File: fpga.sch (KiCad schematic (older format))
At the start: 25 parts, among them IC1 EP4CE10F17, J1 Pinheader_2x5_TH_WALL, U21 EPCS4

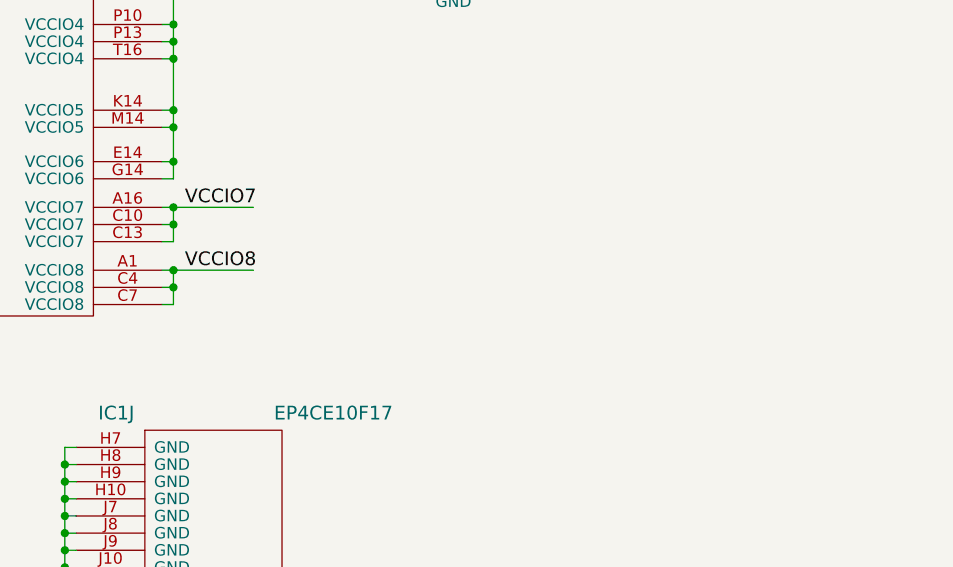
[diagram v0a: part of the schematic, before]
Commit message: Start fitting DDR2
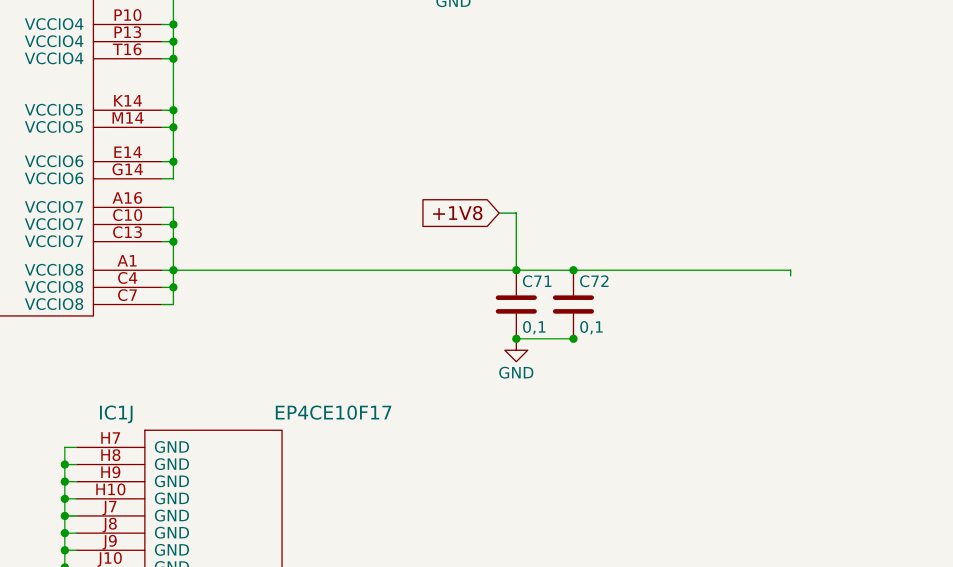
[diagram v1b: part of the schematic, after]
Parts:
- added C71, C72: 0,1, Capacitors_SMD:C_0603, symbol C
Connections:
- net labels added: +1V8
- net labels removed: VCCIO7, VCCIO8
- wire segments 160 -> 163
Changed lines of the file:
@@
 LIBS:Stream
 LIBS:ep4ce10f17
+LIBS:Winbond
 LIBS:Sputnik-cache
 EELAYER 25 0
@@
 $EndComp
 $Comp
-L GND #PWR01
+L GND #PWR6
 U 1 1 5807C448
 P 12075 6725
-F 0 "#PWR01" H 12075 6475 50  0001 C CNN
+F 0 "#PWR6" H 12075 6475 50  0001 C CNN
 F 1 "GND" H 12075 6575 50  0000 C CNN
 F 2 "" H 12075 6725 50  0000 C CNN
@@
 Text GLabel 10525 1600 1    60   Input ~ 0
 VCCINT
-Text Label 12600 3375 0    60   ~ 0
-VCCIO7
-Text Label 12600 3650 0    60   ~ 0
-VCCIO8
 Text Label 10325 3025 0    60   ~ 0
 VCCA1
@@
 $EndComp
 $Comp
-L GND #PWR02
+L GND #PWR5
 U 1 1 57F7A288
 P 2675 3000
-F 0 "#PWR02" H 2675 2750 50  0001 C CNN
+F 0 "#PWR5" H 2675 2750 50  0001 C CNN
 F 1 "GND" H 2675 2850 50  0000 C CNN
 F 2 "" H 2675 3000 50  0000 C CNN
@@
 NoConn ~ 2600 2775
 $Comp
-L +3V3 #PWR03
+L +3V3 #PWR8
 U 1 1 57F8D5C6
 P 13775 2025
-F 0 "#PWR03" H 13875 2075 20  0001 C CNN
+F 0 "#PWR8" H 13875 2075 20  0001 C CNN
 F 1 "+3V3" H 13775 2115 30  0000 C CNN
 F 2 "" H 13775 2025 60  0000 C CNN
@@
 $EndComp
 $Comp
-L GND #PWR04
+L GND #PWR9
 U 1 1 57F8FD8F
 P 13775 2325
-F 0 "#PWR04" H 13775 2075 50  0001 C CNN
+F 0 "#PWR9" H 13775 2075 50  0001 C CNN
 F 1 "GND" H 13775 2175 50  0000 C CNN
 F 2 "" H 13775 2325 50  0000 C CNN
@@
 $EndComp
 $Comp
-L GND #PWR05
+L GND #PWR7
 U 1 1 57F90743
 P 13275 1400
-F 0 "#PWR05" H 13275 1150 50  0001 C CNN
+F 0 "#PWR7" H 13275 1150 50  0001 C CNN
 F 1 "GND" H 13275 1250 50  0000 C CNN
 F 2 "" H 13275 1400 50  0000 C CNN
@@
 Connection ~ 12550 3175
 Wire Wire Line
-	12500 3375 12900 3375
-Wire Wire Line
-	12500 3650 12900 3650
+	12500 3650 15250 3650
 Wire Wire Line
 	12550 3525 12500 3525
 Wire Wire Line
-	12550 3375 12550 3525
-Connection ~ 12550 3375
+	12550 3375 12550 3800
 Wire Wire Line
 	12500 3450 12550 3450
@@
 Wire Wire Line
 	12550 3800 12500 3800
-Wire Wire Line
-	12550 3650 12550 3800
 Connection ~ 12550 3650
 Wire Wire Line
@@
 $EndComp
 $Comp
-L GND #PWR06
+L GND #PWR2
 U 1 1 58612A86
 P 1700 4125
-F 0 "#PWR06" H 1700 3875 50  0001 C CNN
+F 0 "#PWR2" H 1700 3875 50  0001 C CNN
 F 1 "GND" H 1700 3975 50  0000 C CNN
 F 2 "" H 1700 4125 50  0000 C CNN
@@
 $EndComp
 $Comp
-L +3V3 #PWR07
+L +3V3 #PWR3
 U 1 1 586140D5
 P 2650 3775
-F 0 "#PWR07" H 2750 3825 20  0001 C CNN
+F 0 "#PWR3" H 2750 3825 20  0001 C CNN
 F 1 "+3V3" H 2650 3865 30  0000 C CNN
 F 2 "" H 2650 3775 60  0000 C CNN
@@
 Connection ~ 2650 3825
 $Comp
-L +3V3 #PWR08
+L +3V3 #PWR1
 U 1 1 58614C3F
 P 1575 4025
-F 0 "#PWR08" H 1675 4075 20  0001 C CNN
+F 0 "#PWR1" H 1675 4075 20  0001 C CNN
 F 1 "+3V3" H 1575 4115 30  0000 C CNN
 F 2 "" H 1575 4025 60  0000 C CNN
@@
 $EndComp
 $Comp
-L GND #PWR09
+L GND #PWR4
 U 1 1 586161B6
 P 2650 4500
-F 0 "#PWR09" H 2650 4250 50  0001 C CNN
+F 0 "#PWR4" H 2650 4250 50  0001 C CNN
 F 1 "GND" H 2650 4350 50  0000 C CNN
 F 2 "" H 2650 4500 50  0000 C CNN
@@
 Text Label 7050 6050 2    50   ~ 0
 ETHSD14
+$Comp
+L C C71
+U 1 1 5883464A
+P 14050 3800
+F 0 "C71" H 14075 3900 50  0000 L CNN
+F 1 "0,1" H 14075 3700 50  0000 L CNN
+F 2 "Capacitors_SMD:C_0603" H 14088 3650 50  0001 C CNN
+F 3 "" H 14050 3800 50  0000 C CNN
+	1    14050 3800
+	1    0    0    -1
+$EndComp
+$Comp
+L GND #PWR10
+U 1 1 5883481A
+P 14050 3950
+F 0 "#PWR10" H 14050 3700 50  0001 C CNN
+F 1 "GND" H 14050 3800 50  0000 C CNN
+F 2 "" H 14050 3950 50  0000 C CNN
+F 3 "" H 14050 3950 50  0000 C CNN
+	1    14050 3950
+	1    0    0    -1
+$EndComp
+Wire Wire Line
+	15250 3650 15250 3675
+Connection ~ 14050 3650
+Text GLabel 13975 3400 0    60   Input ~ 0
++1V8
+Wire Wire Line
+	13975 3400 14050 3400
+Wire Wire Line
+	14050 3400 14050 3650
+Wire Wire Line
+	12500 3375 12550 3375
+Connection ~ 12550 3525
+$Comp
+L C C72
+U 1 1 588362E2
+P 14300 3800
+F 0 "C72" H 14325 3900 50  0000 L CNN
+F 1 "0,1" H 14325 3700 50  0000 L CNN
+F 2 "Capacitors_SMD:C_0603" H 14338 3650 50  0001 C CNN
+F 3 "" H 14300 3800 50  0000 C CNN
+	1    14300 3800
+	1    0    0    -1
+$EndComp
+Wire Wire Line
+	14300 3950 14050 3950
+Connection ~ 14050 3950
+Connection ~ 14300 3950
+Connection ~ 14300 3650
 $EndSCHEMATC

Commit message: A bit of routing
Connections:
- net labels added: USBAD[0:15]
- net labels removed: VREFB3N0, VREFB4N0, VREFB5N0
- wire segments 163 -> 155
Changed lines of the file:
@@
 $EndComp
 $Comp
-L GND #PWR10
+L GND #PWR01
 U 1 1 5807C448
 P 12075 6725
-F 0 "#PWR10" H 12075 6475 50  0001 C CNN
+F 0 "#PWR01" H 12075 6475 50  0001 C CNN
 F 1 "GND" H 12075 6575 50  0000 C CNN
 F 2 "" H 12075 6725 50  0000 C CNN
@@
 $EndComp
 $Comp
-L GND #PWR4
+L GND #PWR02
 U 1 1 57F7A288
 P 2675 3000
-F 0 "#PWR4" H 2675 2750 50  0001 C CNN
+F 0 "#PWR02" H 2675 2750 50  0001 C CNN
 F 1 "GND" H 2675 2850 50  0000 C CNN
 F 2 "" H 2675 3000 50  0000 C CNN
@@
 NoConn ~ 2600 2775
 $Comp
-L +3V3 #PWR2
+L +3V3 #PWR03
 U 1 1 57F8D5C6
 P 13775 2025
-F 0 "#PWR2" H 13875 2075 20  0001 C CNN
+F 0 "#PWR03" H 13875 2075 20  0001 C CNN
 F 1 "+3V3" H 13775 2115 30  0000 C CNN
 F 2 "" H 13775 2025 60  0000 C CNN
@@
 	1    0    0    -1
 $EndComp
-Text Label 10050 6775 0    60   ~ 0
-VREFB4N0
-Text Label 9525 4625 0    60   ~ 0
-VREFB3N0
 Text Label 9150 2675 0    60   ~ 0
 VREFB2N0
@@
 $EndComp
 $Comp
-L GND #PWR3
+L GND #PWR04
 U 1 1 57F8FD8F
 P 13775 2325
-F 0 "#PWR3" H 13775 2075 50  0001 C CNN
+F 0 "#PWR04" H 13775 2075 50  0001 C CNN
 F 1 "GND" H 13775 2175 50  0000 C CNN
 F 2 "" H 13775 2325 50  0000 C CNN
@@
 $EndComp
 $Comp
-L GND #PWR1
+L GND #PWR05
 U 1 1 57F90743
 P 13275 1400
-F 0 "#PWR1" H 13275 1150 50  0001 C CNN
+F 0 "#PWR05" H 13275 1150 50  0001 C CNN
 F 1 "GND" H 13275 1250 50  0000 C CNN
 F 2 "" H 13275 1400 50  0000 C CNN
@@
 	1    0    0    -1
 $EndComp
-Text Label 9800 8675 0    60   ~ 0
-VREFB5N0
 $Comp
 L C C38
@@
 $EndComp
 $Comp
-L GND #PWR8
+L GND #PWR06
 U 1 1 58612A86
 P 1700 4125
-F 0 "#PWR8" H 1700 3875 50  0001 C CNN
+F 0 "#PWR06" H 1700 3875 50  0001 C CNN
 F 1 "GND" H 1700 3975 50  0000 C CNN
 F 2 "" H 1700 4125 50  0000 C CNN
@@
 $EndComp
 $Comp
-L +3V3 #PWR5
+L +3V3 #PWR07
 U 1 1 586140D5
 P 2650 3775
-F 0 "#PWR5" H 2750 3825 20  0001 C CNN
+F 0 "#PWR07" H 2750 3825 20  0001 C CNN
 F 1 "+3V3" H 2650 3865 30  0000 C CNN
 F 2 "" H 2650 3775 60  0000 C CNN
@@
 Connection ~ 2650 3825
 $Comp
-L +3V3 #PWR7
+L +3V3 #PWR08
 U 1 1 58614C3F
 P 1575 4025
-F 0 "#PWR7" H 1675 4075 20  0001 C CNN
+F 0 "#PWR08" H 1675 4075 20  0001 C CNN
 F 1 "+3V3" H 1575 4115 30  0000 C CNN
 F 2 "" H 1575 4025 60  0000 C CNN
@@
 $EndComp
 $Comp
-L GND #PWR9
+L GND #PWR09
 U 1 1 586161B6
 P 2650 4500
-F 0 "#PWR9" H 2650 4250 50  0001 C CNN
+F 0 "#PWR09" H 2650 4250 50  0001 C CNN
 F 1 "GND" H 2650 4350 50  0000 C CNN
 F 2 "" H 2650 4500 50  0000 C CNN
@@
 Text Label 7050 8550 2    50   ~ 0
 CMD
-Text Label 7050 7425 2    50   ~ 0
-ETHSD8
-Text Label 7050 8100 2    50   ~ 0
-ETHSD9
-Text Label 7050 7500 2    50   ~ 0
-ETHSD10
-Text Label 7050 8775 2    50   ~ 0
-ETHSD11
-Text Label 7050 8850 2    50   ~ 0
-ETHSD12
-Text Label 7050 8700 2    50   ~ 0
-ETHSD13
 Wire Bus Line
 	15100 6725 15100 7925
-Entry Wire Line
-	15100 6925 15200 7025
-Wire Wire Line
-	15200 7025 15600 7025
-Entry Wire Line
-	15100 7025 15200 7125
-Entry Wire Line
-	15100 7125 15200 7225
-Entry Wire Line
-	15100 7225 15200 7325
-Entry Wire Line
-	15100 7325 15200 7425
-Entry Wire Line
-	15100 7425 15200 7525
-Entry Wire Line
-	15100 7525 15200 7625
-Entry Wire Line
-	15100 7625 15200 7725
-Wire Wire Line
-	15200 7125 15600 7125
-Wire Wire Line
-	15200 7225 15600 7225
-Wire Wire Line
-	15200 7325 15600 7325
-Wire Wire Line
-	15200 7425 15600 7425
-Wire Wire Line
-	15200 7525 15600 7525
-Wire Wire Line
-	15200 7625 15600 7625
-Wire Wire Line
-	15200 7725 15600 7725
-Text Label 15600 7225 2    50   ~ 0
-ETHSD13
-Text Label 15600 7325 2    50   ~ 0
-ETHSD12
-Text Label 15600 7425 2    50   ~ 0
-ETHSD11
-Text Label 15600 7525 2    50   ~ 0
-ETHSD10
-Text Label 7050 6425 2    50   ~ 0
-ETHSD7
-Text Label 7050 5450 2    50   ~ 0
-ETHSD6
-Text Label 7050 5375 2    50   ~ 0
-ETHSD5
-Text Label 7050 5300 2    50   ~ 0
-ETHSD4
-Text Label 7050 6950 2    50   ~ 0
-ETHSD3
-Text Label 7050 6875 2    50   ~ 0
-ETHSD2
-Text Label 7050 7875 2    50   ~ 0
-ETHSD1
-Text Label 7050 6125 2    50   ~ 0
-ETHSD0
-Text Label 7050 8325 2    50   ~ 0
-ETHSD15
-Text Label 7050 6050 2    50   ~ 0
-ETHSD14
 $Comp
 L C C71
@@
 $EndComp
 $Comp
-L GND #PWR6
+L GND #PWR010
 U 1 1 5883481A
 P 14050 3950
-F 0 "#PWR6" H 14050 3700 50  0001 C CNN
+F 0 "#PWR010" H 14050 3700 50  0001 C CNN
 F 1 "GND" H 14050 3800 50  0000 C CNN
 F 2 "" H 14050 3950 50  0000 C CNN
@@
 Connection ~ 14300 3950
 Connection ~ 14300 3650
+Text HLabel 15100 8275 2    60   BiDi ~ 0
+USBAD[0:15]
+Text GLabel 7050 8850 0    39   Input ~ 0
+ETHSD12
+Text GLabel 7050 8775 0    39   Input ~ 0
+ETHSD11
+Text GLabel 7050 8700 0    39   Input ~ 0
+ETHSD13
+Text GLabel 7050 8325 0    39   Input ~ 0
+ETHSD15
+Text GLabel 7050 7500 0    39   Input ~ 0
+ETHSD10
+Text GLabel 7050 7875 0    39   Input ~ 0
+ETHSD1
+Text GLabel 7050 8100 0    39   Input ~ 0
+ETHSD9
+Text GLabel 7050 7425 0    39   Input ~ 0
+ETHSD8
+Text GLabel 7050 6950 0    39   Input ~ 0
+ETHSD3
+Text GLabel 7050 6875 0    39   Input ~ 0
+ETHSD2
+Text GLabel 7050 6425 0    39   Input ~ 0
+ETHSD7
+Text GLabel 7050 6125 0    39   Input ~ 0
+ETHSD0
+Text GLabel 7050 6050 0    39   Input ~ 0
+ETHSD14
+Text GLabel 7050 5450 0    39   Input ~ 0
+ETHSD6
+Text GLabel 7050 5375 0    39   Input ~ 0
+ETHSD5
+Text GLabel 7050 5300 0    39   Input ~ 0
+ETHSD4
 $EndSCHEMATC

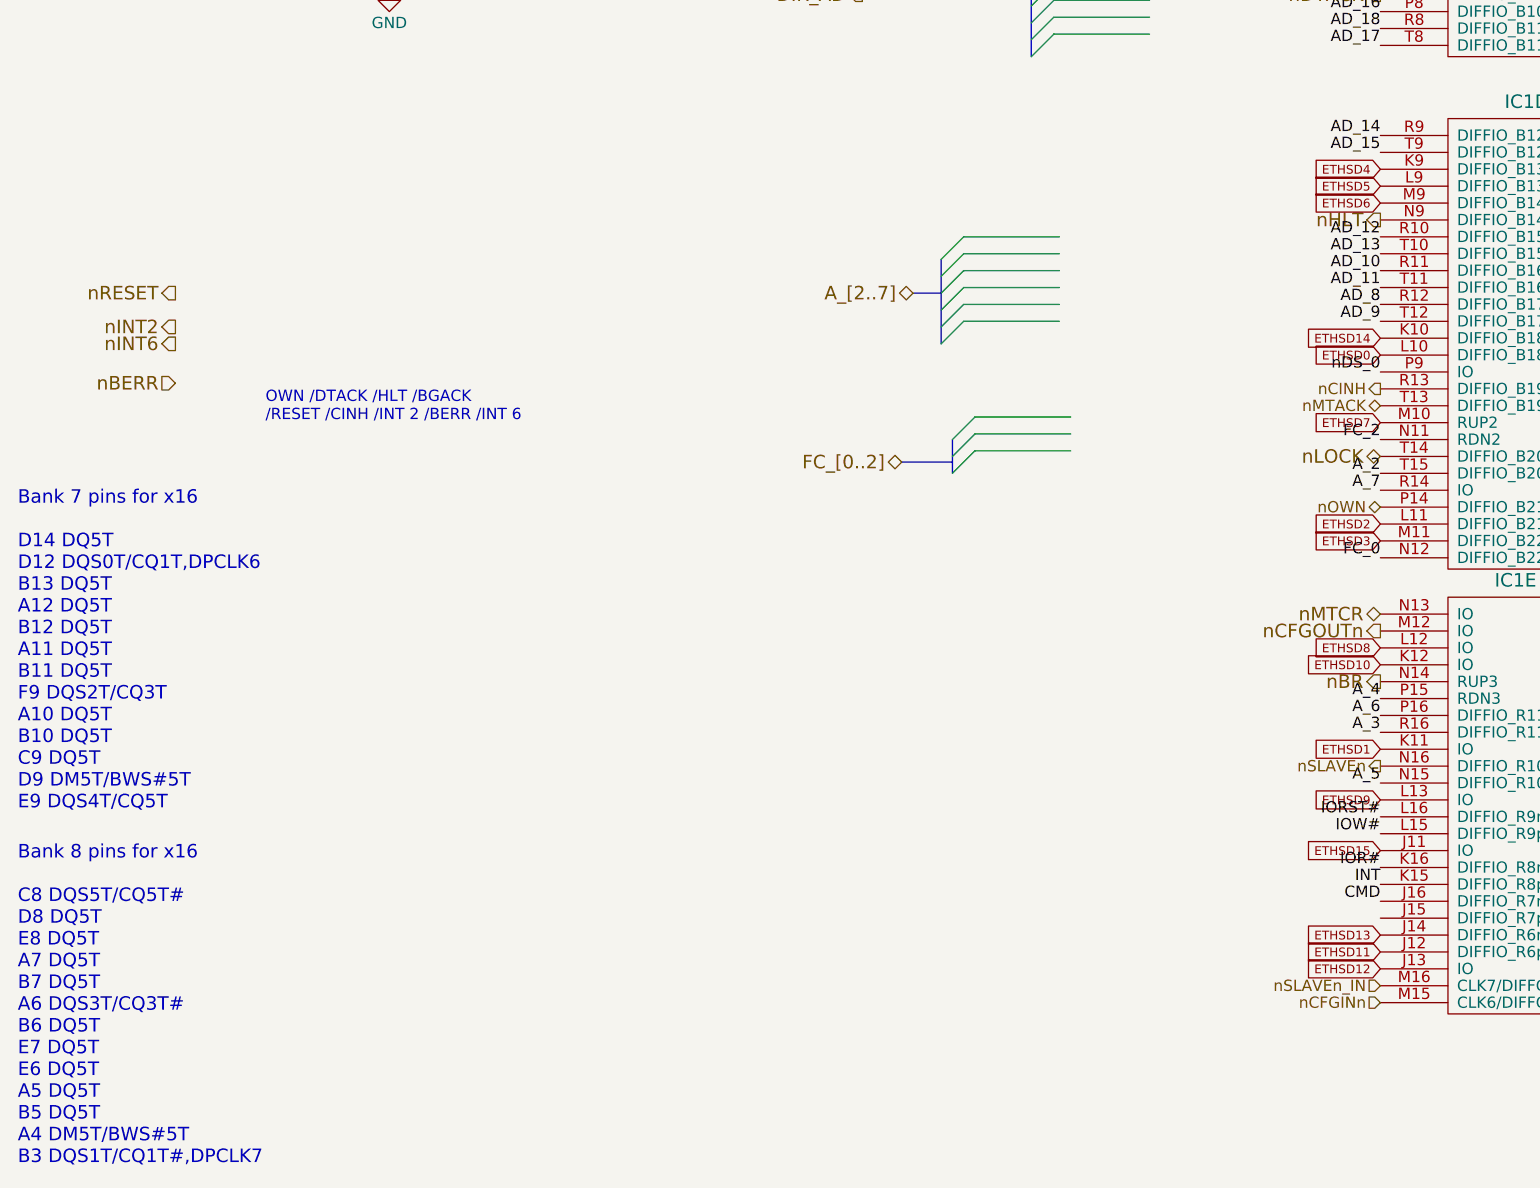
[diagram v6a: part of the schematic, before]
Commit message: USB/Ethernet AD tracks swapped and routed
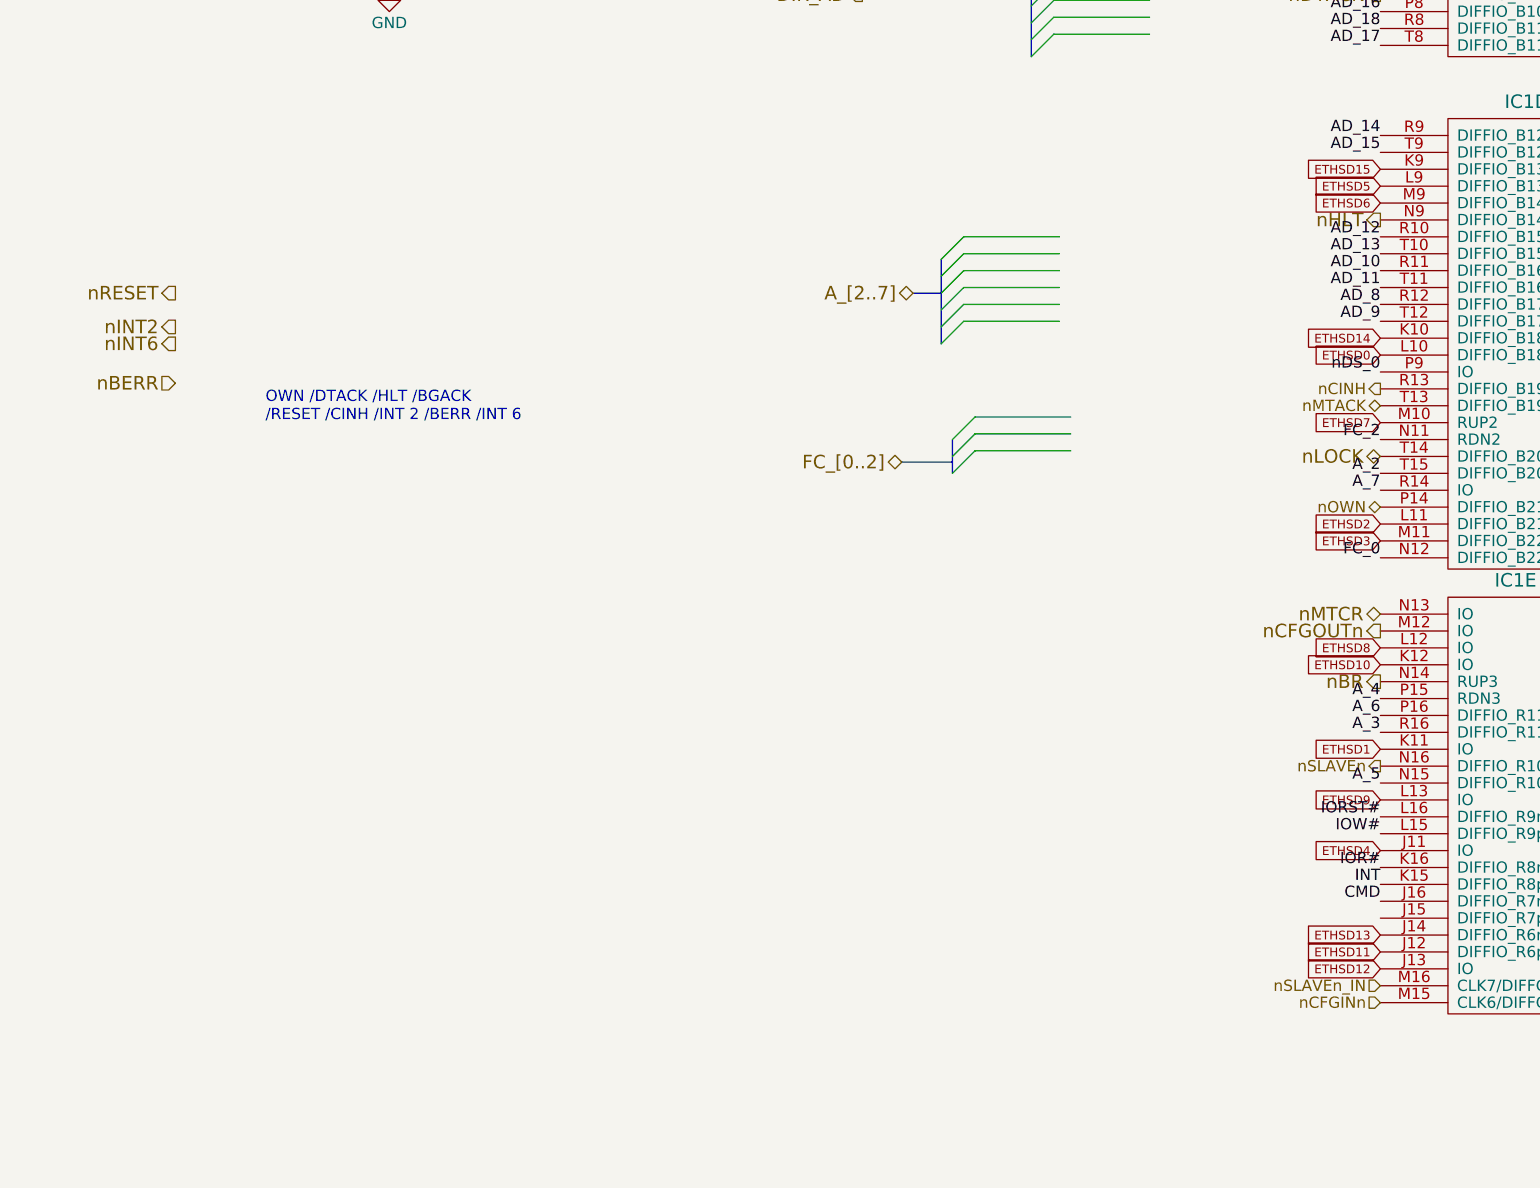
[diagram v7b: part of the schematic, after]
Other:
- note removed: "Bank 7 pins for x16\n\nD14 DQ5T\nD12 DQS0T/CQ1T,DPCLK6\nB13 DQ5T\nA12 DQ5T\nB12 DQ5T\nA11 DQ5T\nB11 DQ5T\nF9 DQS2T/CQ3T\nA10 DQ5T\nB10 DQ5T\nC9 DQ5T\nD9 DM5T/BWS#5T\nE9 DQS4T/CQ5T"
- note removed: "Bank 8 pins for x16\n\nC8 DQS5T/CQ5T#\nD8 DQ5T\nE8 DQ5T\nA7 DQ5T\nB7 DQ5T\nA6 DQS3T/CQ3T#\nB6 DQ5T\nE7 DQ5T\nE6 DQ5T\nA5 DQ5T\nB5 DQ5T\nA4 DM5T/BWS#5T\nB3 DQS1T/CQ1T#,DPCLK7"
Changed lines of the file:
@@
 	1    0    0    -1
 $EndComp
-Text Notes 1000 9725 0    60   ~ 0
-Bank 8 pins for x16\n\nC8 DQS5T/CQ5T#\nD8 DQ5T\nE8 DQ5T\nA7 DQ5T\nB7 DQ5T\nA6 DQS3T/CQ3T#\nB6 DQ5T\nE7 DQ5T\nE6 DQ5T\nA5 DQ5T\nB5 DQ5T\nA4 DM5T/BWS#5T\nB3 DQS1T/CQ1T#,DPCLK7
-Text Notes 1000 8150 0    60   ~ 0
-Bank 7 pins for x16\n\nD14 DQ5T\nD12 DQS0T/CQ1T,DPCLK6\nB13 DQ5T\nA12 DQ5T\nB12 DQ5T\nA11 DQ5T\nB11 DQ5T\nF9 DQS2T/CQ3T\nA10 DQ5T\nB10 DQ5T\nC9 DQ5T\nD9 DM5T/BWS#5T\nE9 DQS4T/CQ5T
 Text HLabel 7050 8925 0    50   Input ~ 0
 nSLAVEn_IN
@@
 Text GLabel 7050 8700 0    39   Input ~ 0
 ETHSD13
-Text GLabel 7050 8325 0    39   Input ~ 0
-ETHSD15
 Text GLabel 7050 7500 0    39   Input ~ 0
 ETHSD10
@@
 Text GLabel 7050 5375 0    39   Input ~ 0
 ETHSD5
+Text GLabel 7050 8325 0    39   Input ~ 0
+ETHSD4
 Text GLabel 7050 5300 0    39   Input ~ 0
-ETHSD4
+ETHSD15
 $EndSCHEMATC
